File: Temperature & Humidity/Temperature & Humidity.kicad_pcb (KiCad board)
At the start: 2 copper layers, 59.9 x 50 mm, 18 parts, among them U1 ESP32-C3-MINI-1, U2 SHT4x, U3 MIC5504-3.3YM5

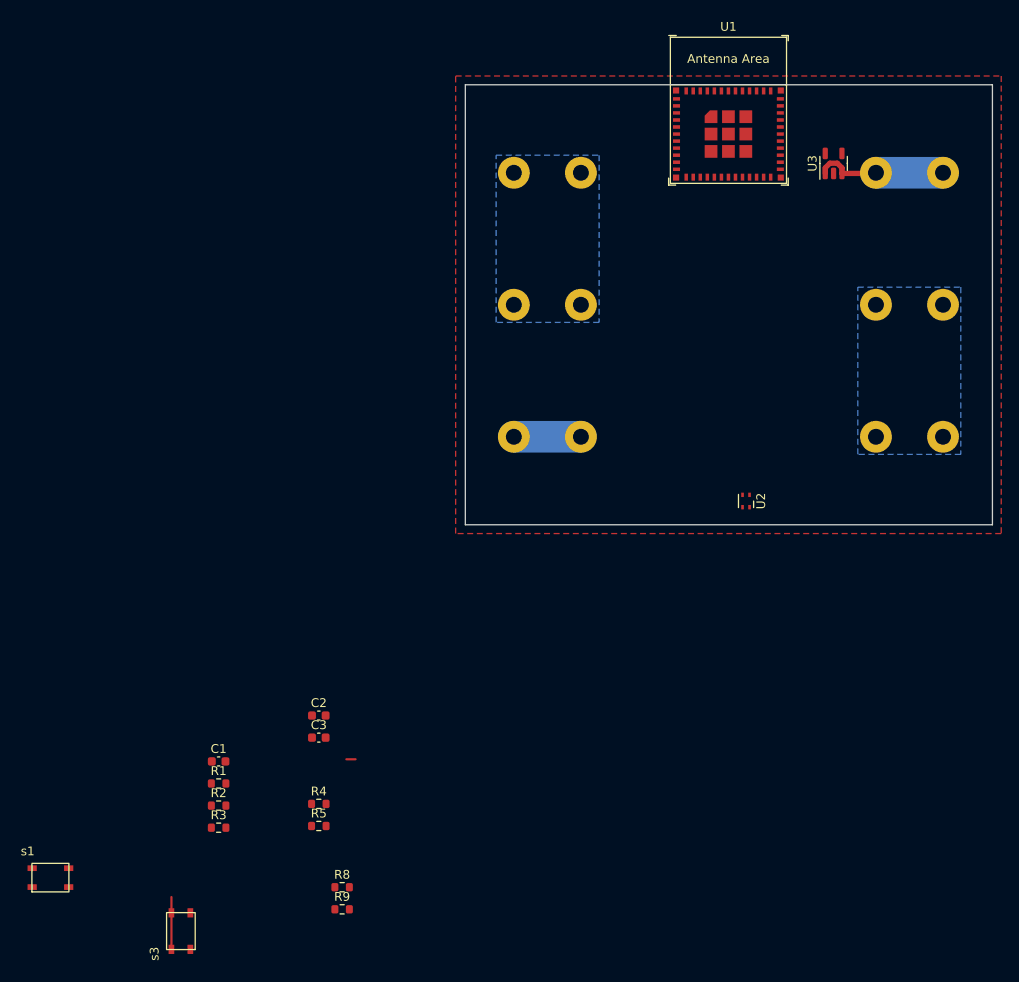
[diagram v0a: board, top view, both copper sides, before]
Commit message: added battery level sensor
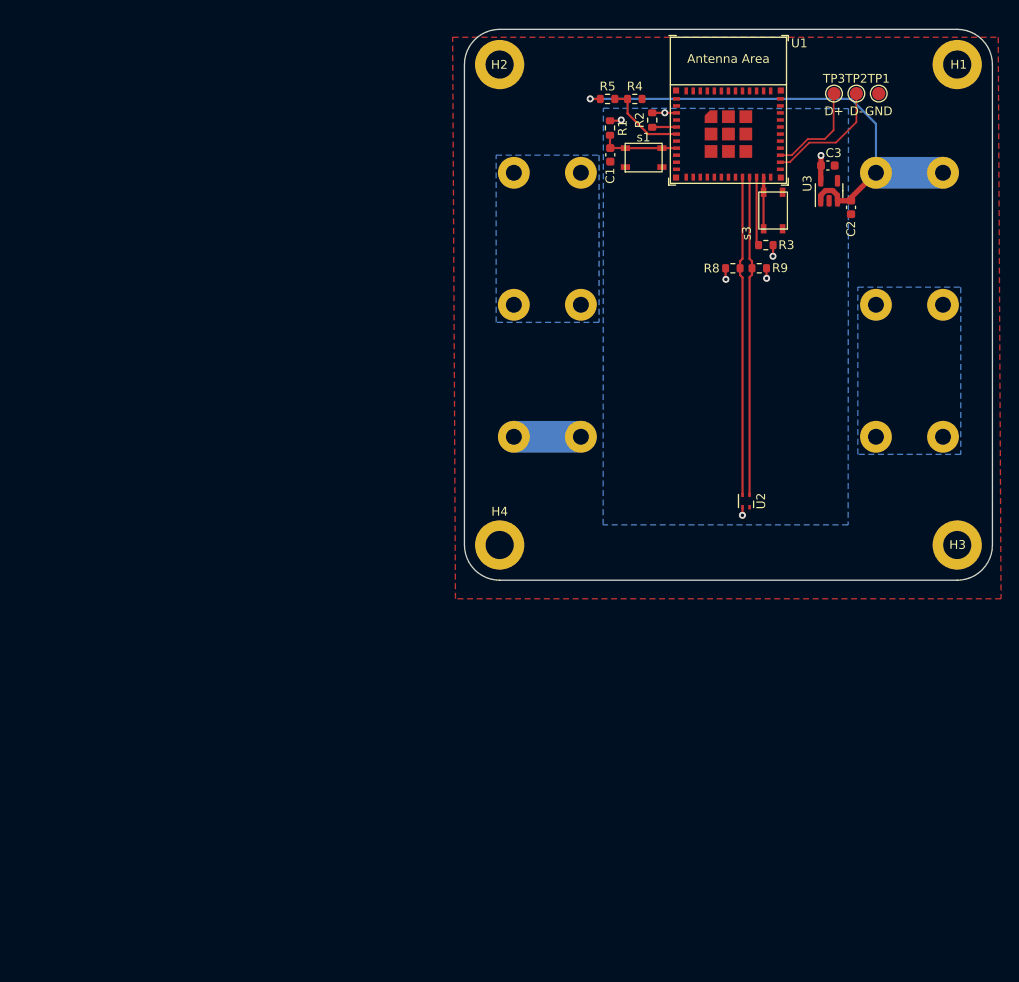
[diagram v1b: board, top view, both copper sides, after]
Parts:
- added H1: MountingHole, MountingHole:MountingHole_3.2mm_M3_DIN965_Pad, F.Cu at (140.3, 27.8)
- added H2: MountingHole, MountingHole:MountingHole_3.2mm_M3_DIN965_Pad, F.Cu at (88.3, 27.8)
- added H3: MountingHole, MountingHole:MountingHole_3.2mm_M3_DIN965_Pad, F.Cu at (140.3, 82.4)
- added H4: MountingHole, MountingHole:MountingHole_3.2mm_M3_DIN965_Pad, F.Cu at (88.3, 82.4)
- added TP1: TestPoint, TestPoint:TestPoint_Pad_D1.5mm, F.Cu at (131.4, 31.1)
- added TP2: TestPoint, TestPoint:TestPoint_Pad_D1.5mm, F.Cu at (128.8, 31.1)
- added TP3: TestPoint, TestPoint:TestPoint_Pad_D1.5mm, F.Cu at (126.3, 31.1)
- R4: value 5k1 -> 125k
- R5: value 5k1 -> 100k
- moved s1 106.0 mm to (104.7, 38.4)
- moved s3 106.0 mm to (119.4, 44.4)
- moved R2 92.2 mm to (105.6, 34.1), turned to 90 degrees
- moved R3 90.8 mm to (118.5, 48.3), turned to 180 degrees
- moved R5 88.9 mm to (100.6, 31.7)
- moved R4 87.8 mm to (103.7, 31.7)
- moved C3 87.0 mm to (125.6, 39.3)
- moved R9 86.9 mm to (117.8, 51.0)
- moved R1 86.8 mm to (100.8, 35.0), turned to -90 degrees
- moved C2 83.6 mm to (128.2, 44.0), turned to -90 degrees
- moved R8 83.2 mm to (114.8, 51.0), turned to 180 degrees
- moved C1 82.1 mm to (100.9, 38.1), turned to -90 degrees
- moved U3 3.15 mm to (125.7, 42.1)
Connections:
- R4 pad 1: Net-(USB-C1-CC2) -> ADC
- R5 pad 1: Net-(USB-C1-CC1) -> +3V8
- R5 pad 2: GND -> ADC
- U1 pad 6: unconnected-(U1-GPIO3/ADC1_CH3-Pad6) -> ADC
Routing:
- net +3V8: track 15.1 -> 57.3 mm, vias 0 -> 1
- net SDA: track 0.00 -> 36.3 mm
- net SCL: track 0.00 -> 36.3 mm
- net USB_D-: track 0.00 -> 13.8 mm
- net +3V3: track 0.00 -> 11.6 mm, vias 0 -> 7
- net USB_D+: track 0.00 -> 11.4 mm
- net ADC: track 0.00 -> 9.62 mm
- net Net-(U1-EN/CHIP_PU): track 0.00 -> 9.00 mm
- net Net-(U1-GPIO8): track 0.00 -> 7.81 mm
- net Net-(U1-GPIO2/ADC1_CH2): track 0.00 -> 2.77 mm
- net GND: track 8.67 -> 7.62 mm
- added copper zone on B.Cu, net +3V3
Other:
- board size 59.9 x 50 mm -> 60 x 62.6 mm
- board text added: "D+"
- board text added: "D-"
- board text added: "GND"
